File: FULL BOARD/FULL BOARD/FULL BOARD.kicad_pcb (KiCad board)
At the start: 2 copper layers, 200 x 200 mm, 113 parts, among them IC1 TAS5760LDAP, J1 PJ-036AH-SMT-TR, J2 Micro_SD_Card, J3 B2B-PH-K-S, J4 5019514000, J5 61201021621, J6 B2B-PH-K-S, SW1 PTS645SK50SMTR92LFS, U1 LD1117S33TR_SOT223, U2 STM32H743VITx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

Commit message: parts moved
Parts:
- moved J4 68.4 mm to (251.3, 100.4), turned to -90 degrees
- moved J2 52.0 mm to (196.2, 53.8)
- moved C1 45.9 mm to (202.4, 65.4), turned to 0 degrees
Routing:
- net +5V: track 299.4 -> 397.5 mm
- net /SD_DO: track 118.8 -> 64.0 mm
- net /LCD_MOSI: track 50.5 -> 102.3 mm
- net /SD_CLK: track 121.8 -> 70.0 mm
- net /LCD_MISO: track 50.5 -> 101.6 mm
- net Wait: track 53.2 -> 102.6 mm
- net /LCD_CS: track 49.7 -> 97.8 mm
- net /SD_CS: track 125.4 -> 78.3 mm
- net /SD_DI: track 109.3 -> 62.2 mm
- net /LCD_SCK: track 50.9 -> 97.4 mm
- net +3.3V: track 583.7 -> 618.9 mm
- net GND: track 145.4 -> 125.7 mm
- net /NRST: track 126.0 -> 120.4 mm
- net +3.3VA: track 56.4 -> 58.9 mm
- net GNDA: track 38.8 -> 38.1 mm

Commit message: added names
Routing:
- net GND: track 125.7 -> 126.8 mm
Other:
- board text added: "ECE 477 Group 7 Conundrum Crack V 1.0 Colby Acton Joseph Eisenberg Aloysius Rebeiro Andrew Pohl"

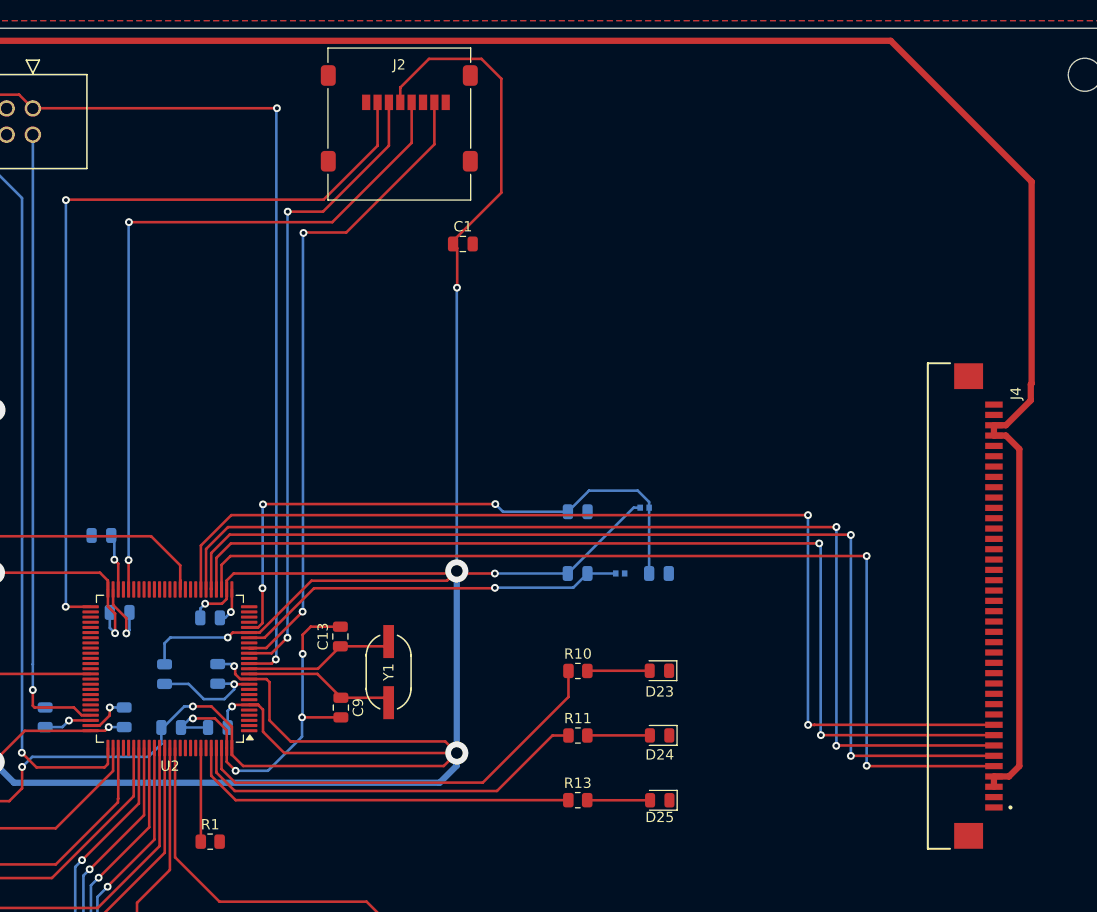
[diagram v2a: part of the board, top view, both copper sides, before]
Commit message: moved sd and lcd
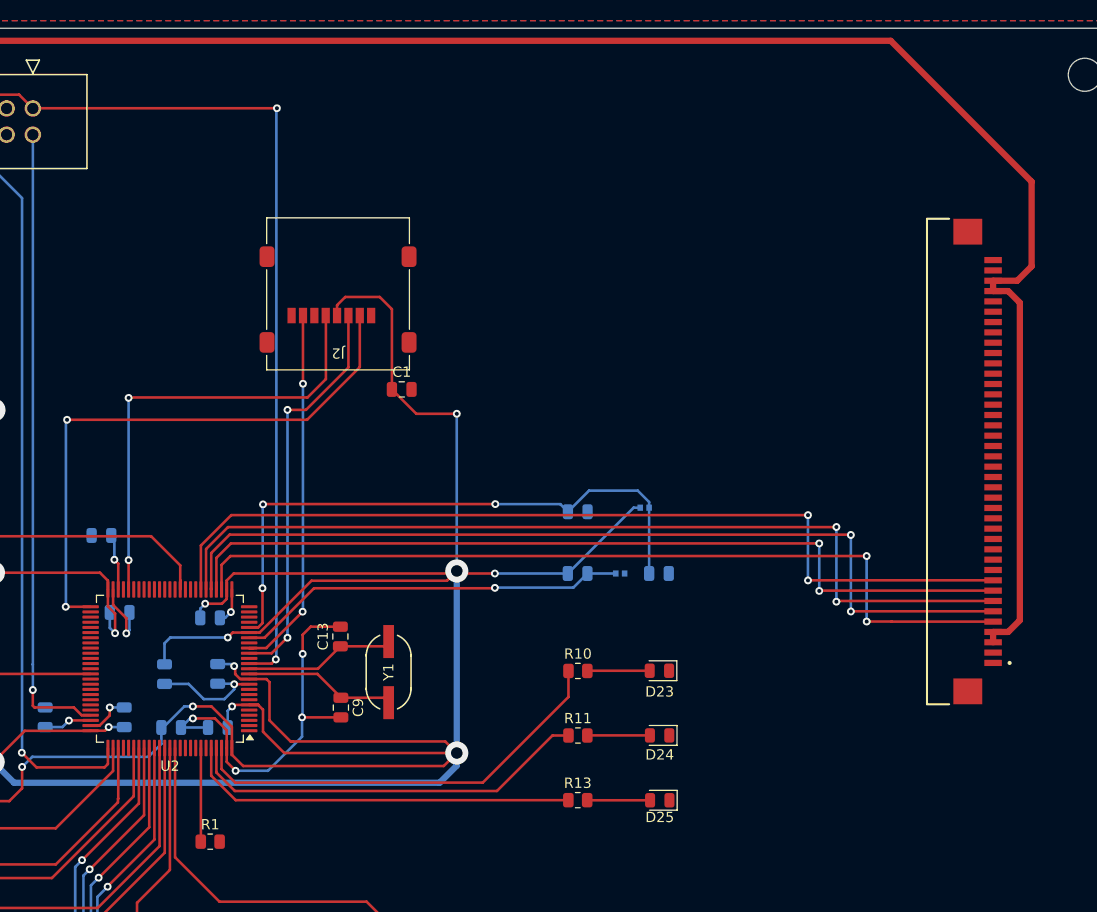
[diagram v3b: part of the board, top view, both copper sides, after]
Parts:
- moved J2 17.5 mm to (190.3, 70.2), turned to 180 degrees
- moved C1 15.3 mm to (196.5, 79.5)
- moved J4 14.0 mm to (251.3, 86.4)
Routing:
- net /SD_DO: track 64.0 -> 35.7 mm
- net /SD_CLK: track 70.0 -> 44.6 mm
- net +3.3V: track 618.9 -> 593.5 mm
- net /SD_DI: track 62.2 -> 39.1 mm
- net /SD_CS: track 78.3 -> 56.0 mm
- net Wait: track 102.6 -> 88.5 mm
- net /LCD_MISO: track 101.6 -> 87.5 mm
- net /LCD_CS: track 97.8 -> 83.8 mm
- net /LCD_MOSI: track 102.3 -> 88.2 mm
- net /LCD_SCK: track 97.4 -> 83.7 mm
- net +5V: track 397.5 -> 384.5 mm

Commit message: moved parts
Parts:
- moved C1 1.16 mm to (196.5, 80.6)
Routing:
- net +3.3V: track 593.5 -> 594.5 mm
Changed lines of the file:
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@@
 	(footprint "Capacitor_SMD:C_0805_2012Metric"
 		(layer "F.Cu")
-		(at 196.47 79.46)
+		(at 196.47 80.62)
 		(descr "Capacitor SMD 0805 (2012 Metric), square (rectangular) end terminal, IPC_7351 nominal, (Body size source: IPC-SM-782 page 76, https://www.pcb-3d.com/wordpress/wp-content/uploads/ipc-sm-782a_amendment_1_and_2.pdf, https://docs.google.com/spreadsheets/d/1BsfQQcO9C6DZCsRaXUlFlo91Tg2WpOkGARC1WS5S8t0/edit?usp=sharing), generated with kicad-footprint-generator")
 		(tags "capacitor")
@@
 	)
 	(segment
-		(start 194.34 70.51)
-		(end 191.006 70.51)
-		(width 0.254)
-		(layer "F.Cu")
-		(net 1)
-	)
-	(segment
 		(start 104.71 131.65)
 		(end 104.7068 131.6532)
@@
 	)
 	(segment
+		(start 190.21 71.306)
+		(end 190.21 72.31)
+		(width 0.254)
+		(layer "F.Cu")
+		(net 1)
+	)
+	(segment
 		(start 89.591 75.1888)
 		(end 89.591 71.7246)
@@
 	)
 	(segment
-		(start 201.8 81.82)
-		(end 197.88 81.82)
+		(start 195.52 80.62)
+		(end 195.52 71.69)
 		(width 0.254)
 		(layer "F.Cu")
@@
 	)
 	(segment
-		(start 195.52 71.69)
-		(end 194.34 70.51)
+		(start 201.5528 97.282)
+		(end 180.200408 97.282)
 		(width 0.254)
 		(layer "F.Cu")
@@
 	)
 	(segment
-		(start 201.5528 97.282)
-		(end 180.200408 97.282)
+		(start 195.52 81.47)
+		(end 195.52 80.62)
 		(width 0.254)
 		(layer "F.Cu")
@@
 	)
 	(segment
-		(start 197.88 81.82)
-		(end 195.52 79.46)
+		(start 194.34 70.51)
+		(end 191.006 70.51)
 		(width 0.254)
 		(layer "F.Cu")
@@
 	)
 	(segment
+		(start 191.006 70.51)
+		(end 190.21 71.306)
+		(width 0.254)
+		(layer "F.Cu")
+		(net 1)
+	)
+	(segment
 		(start 180.831408 107.501)
 		(end 181.702 107.501)
@@
 	)
 	(segment
-		(start 191.006 70.51)
-		(end 190.21 71.306)
-		(width 0.254)
-		(layer "F.Cu")
-		(net 1)
-	)
-	(segment
 		(start 182.572592 110.001)
 		(end 181.702 110.001)
@@
 	)
 	(segment
+		(start 195.52 71.69)
+		(end 194.34 70.51)
+		(width 0.254)
+		(layer "F.Cu")
+		(net 1)
+	)
+	(segment
 		(start 180.027 112.127)
 		(end 180.027 114.176)
@@
 	)
 	(segment
-		(start 195.52 79.46)
-		(end 195.52 71.69)
+		(start 185.1 114.66)
+		(end 183.04 112.6)
 		(width 0.254)
 		(layer "F.Cu")
@@
 	)
 	(segment
-		(start 185.1 114.66)
-		(end 183.04 112.6)
+		(start 181.702 103.001)
+		(end 182.714645 103.001)
 		(width 0.254)
 		(layer "F.Cu")
@@
 	)
 	(segment
-		(start 181.702 103.001)
-		(end 182.714645 103.001)
+		(start 201.8 82.02)
+		(end 196.07 82.02)
 		(width 0.254)
 		(layer "F.Cu")
@@
 	)
 	(segment
-		(start 190.21 71.306)
-		(end 190.21 72.31)
+		(start 196.07 82.02)
+		(end 195.52 81.47)
 		(width 0.254)
 		(layer "F.Cu")
@@
 	)
 	(via
-		(at 201.8 81.82)
+		(at 201.8 82.02)
 		(size 0.762)
 		(drill 0.381)
@@
 	)
 	(segment
-		(start 201.8 97.0348)
-		(end 201.8 81.82)
-		(width 0.254)
-		(layer "B.Cu")
-		(net 1)
-	)
-	(segment
 		(start 201.8 115.88)
 		(end 200.14 117.54)
@@
 		(width 0.254)
 		(layer "B.Cu")
+		(net 1)
+	)
+	(segment
+		(start 201.8 97.0348)
+		(end 201.8 82.02)
+		(width 0.254)
+		(layer "B.Cu")

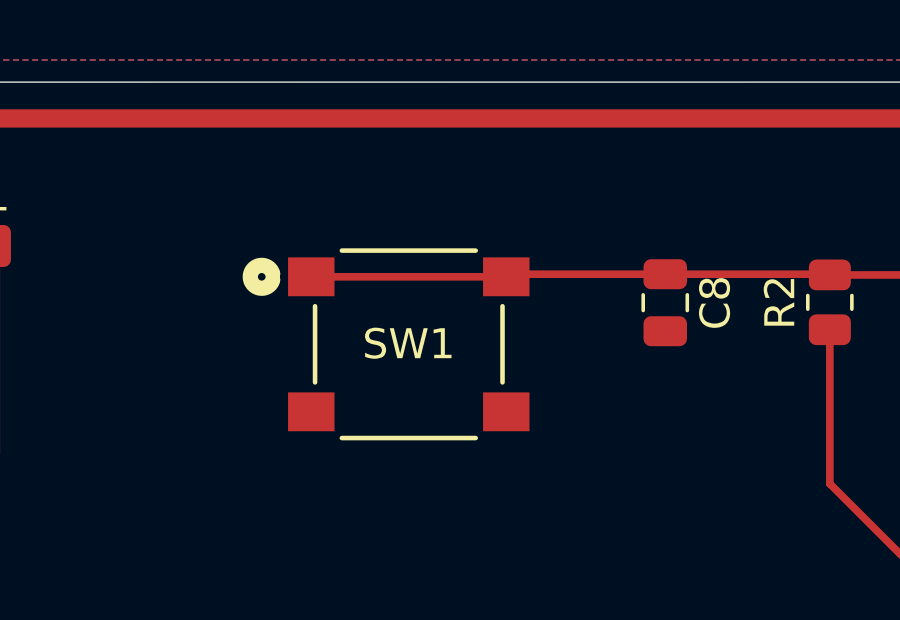
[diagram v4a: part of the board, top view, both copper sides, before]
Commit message: changed reset footprint
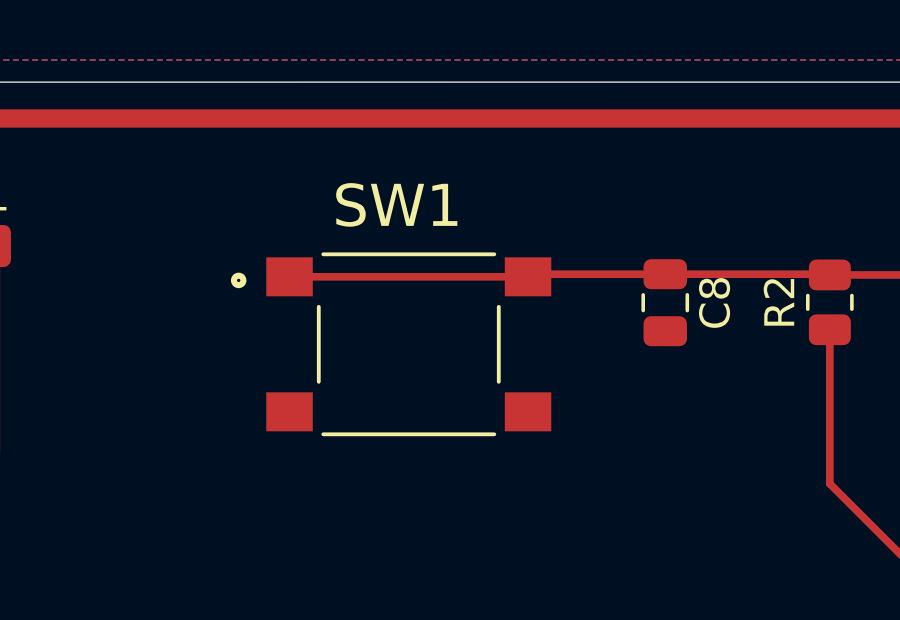
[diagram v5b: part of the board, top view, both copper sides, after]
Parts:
- SW1: footprint push button custom:SW4_PTS645SK50SMTR92LFS_CNK -> Reset Switch:SW_PTS645SK50SMTR92LFS
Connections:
- IC1 pad V: GND -> (no net)
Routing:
- net /NRST: track 120.4 -> 121.1 mm
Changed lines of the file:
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@@
 			(layers "*.Cu" "*.Mask")
 			(remove_unused_layers no)
-			(net 2 "GND")
 		)
 		(model "Z:/Downloads/school/477/KiCAD/PCB-Conundrum-Crack/Footprints/ul_TAS5760LDAP/KiCADv6/TAS5760LDAP.step"
@@
 		)
 	)
-	(footprint "push button custom:SW4_PTS645SK50SMTR92LFS_CNK"
+	(footprint "Reset Switch:SW_PTS645SK50SMTR92LFS"
 		(layer "F.Cu")
 		(at 123.9884 53.2386)
-		(tags "PTS645SK50SMTR92LFS ")
 		(property "Reference" "SW1"
-			(at 0 0 0)
-			(unlocked yes)
+			(at -0.375575 -4.596095 0)
 			(layer "F.SilkS")
 			(effects
 				(font
-					(size 1 1)
+					(size 1.402165 1.402165)
 					(thickness 0.15)
 				)
@@
 		)
 		(property "Value" "PTS645SK50SMTR92LFS"
-			(at 0.1016 5.5914 0)
-			(unlocked yes)
+			(at 15.23461 4.368615 0)
 			(layer "F.Fab")
 			(effects
 				(font
-					(size 1 1)
+					(size 1.402449 1.402449)
 					(thickness 0.15)
 				)
 			)
 		)
-		(property "Footprint" "push button custom:SW4_PTS645SK50SMTR92LFS_CNK"
+		(property "Footprint" "Reset Switch:SW_PTS645SK50SMTR92LFS"
 			(at 0 0 0)
 			(layer "F.Fab")
@@
 		(sheetfile "FULL BOARD.kicad_sch")
 		(attr smd)
-		(fp_circle
-			(center -4.9022 -2.250001)
-			(end -4.5212 -2.250001)
-			(stroke
-				(width 0.508)
-				(type solid)
-			)
-			(fill none)
-			(layer "B.SilkS")
-		)
 		(fp_line
-			(start -3.1242 -1.269561)
-			(end -3.1242 1.269561)
+			(start -3 -1.25)
+			(end -3 1.25)
 			(stroke
-				(width 0.1524)
+				(width 0.127)
 				(type solid)
 			)
@@
 		)
 		(fp_line
-			(start -2.231551 3.1242)
-			(end 2.231551 3.1242)
+			(start -2.85 -3)
+			(end 2.85 -3)
 			(stroke
-				(width 0.1524)
+				(width 0.127)
 				(type solid)
 			)
@@
 		)
 		(fp_line
-			(start 2.231551 -3.1242)
-			(end -2.231551 -3.1242)
+			(start -2.85 3)
+			(end 2.85 3)
 			(stroke
-				(width 0.1524)
+				(width 0.127)
 				(type solid)
 			)
@@
 		)
 		(fp_line
-			(start 3.1242 1.269561)
-			(end 3.1242 -1.269561)
+			(start 3 -1.25)
+			(end 3 1.25)
 			(stroke
-				(width 0.1524)
+				(width 0.127)
 				(type solid)
 			)
 			(layer "F.SilkS")
 		)
-		(fp_arc
-			(start -4.535241 -2.14752)
-			(mid -5.2832 -2.250001)
-			(end -4.535241 -2.352481)
+		(fp_circle
+			(center -5.67 -2.13)
+			(end -5.511888 -2.13)
 			(stroke
-				(width 0.508)
+				(width 0.2)
 				(type solid)
 			)
+			(fill none)
 			(layer "F.SilkS")
 		)
 		(fp_line
-			(start -4.278699 -3.2512)
-			(end -4.278699 3.2512)
+			(start -5 -3.25)
+			(end 5 -3.25)
 			(stroke
-				(width 0.1524)
+				(width 0.05)
 				(type solid)
 			)
@@
 		)
 		(fp_line
-			(start -4.278699 3.2512)
-			(end 4.278699 3.2512)
+			(start -5 3.25)
+			(end -5 -3.25)
 			(stroke
-				(width 0.1524)
+				(width 0.05)
 				(type solid)
 			)
@@
 		)
 		(fp_line
-			(start 4.278699 -3.2512)
-			(end -4.278699 -3.2512)
+			(start 5 -3.25)
+			(end 5 3.25)
 			(stroke
-				(width 0.1524)
+				(width 0.05)
 				(type solid)
 			)
@@
 		)
 		(fp_line
-			(start 4.278699 3.2512)
-			(end 4.278699 -3.2512)
+			(start 5 3.25)
+			(end -5 3.25)
 			(stroke
-				(width 0.1524)
+				(width 0.05)
 				(type solid)
 			)
@@
 		)
 		(fp_line
-			(start -2.9972 -2.9972)
-			(end -2.9972 2.9972)
+			(start -3 -3)
+			(end 3 -3)
 			(stroke
-				(width 0.0254)
+				(width 0.127)
 				(type solid)
 			)
@@
 		)
 		(fp_line
-			(start -2.9972 2.9972)
-			(end 2.9972 2.9972)
+			(start -3 3)
+			(end -3 -3)
 			(stroke
-				(width 0.0254)
+				(width 0.127)
 				(type solid)
 			)
@@
 		)
 		(fp_line
-			(start 2.9972 -2.9972)
-			(end -2.9972 -2.9972)
+			(start 3 -3)
+			(end 3 3)
 			(stroke
-				(width 0.0254)
+				(width 0.127)
 				(type solid)
 			)
@@
 		)
 		(fp_line
-			(start 2.9972 2.9972)
-			(end 2.9972 -2.9972)
+			(start 3 3)
+			(end -3 3)
 			(stroke
-				(width 0.0254)
+				(width 0.127)
 				(type solid)
 			)
@@
 		)
 		(fp_circle
-			(center -3.250001 -4.155001)
-			(end -2.869001 -4.155001)
+			(center -2.368 -2.257)
+			(end -2.209888 -2.257)
 			(stroke
-				(width 0.508)
+				(width 0.2)
 				(type solid)
 			)
@@
 			(layer "F.Fab")
 		)
-		(fp_text user "${REFERENCE}"
-			(at 0 0 0)
-			(unlocked yes)
-			(layer "F.Fab")
-			(effects
-				(font
-					(size 1 1)
-					(thickness 0.15)
-				)
-			)
-		)
 		(pad "1" smd rect
-			(at -3.250001 -2.250001)
-			(size 1.5494 1.2954)
+			(at -3.975 -2.25)
+			(size 1.55 1.3)
 			(layers "F.Cu" "F.Paste" "F.Mask")
 			(net 6 "/NRST")
 			(pinfunction "1")
 			(pintype "unspecified")
+			(solder_mask_margin 0.102)
 		)
 		(pad "2" smd rect
-			(at 3.250001 -2.250001)
-			(size 1.5494 1.2954)
+			(at 3.975 -2.25)
+			(size 1.55 1.3)
 			(layers "F.Cu" "F.Paste" "F.Mask")
 			(net 6 "/NRST")
 			(pinfunction "2")
 			(pintype "unspecified")
+			(solder_mask_margin 0.102)
 		)
 		(pad "3" smd rect
-			(at -3.250001 2.250001)
-			(size 1.5494 1.2954)
+			(at -3.975 2.25)
+			(size 1.55 1.3)
 			(layers "F.Cu" "F.Paste" "F.Mask")
 			(net 2 "GND")
 			(pinfunction "3")
 			(pintype "unspecified")
+			(solder_mask_margin 0.102)
 		)
 		(pad "4" smd rect
-			(at 3.250001 2.250001)
-			(size 1.5494 1.2954)
+			(at 3.975 2.25)
+			(size 1.55 1.3)
 			(layers "F.Cu" "F.Paste" "F.Mask")
 			(net 2 "GND")
 			(pinfunction "4")
 			(pintype "unspecified")
+			(solder_mask_margin 0.102)
 		)
 	)
@@
 		(tags "capacitor")
 		(property "Reference" "C1"
-			(at 0 -1.68 360)
+			(at 0 -1.68 0)
 			(layer "F.SilkS")
 			(effects
@@
 		)
 		(property "Value" "100uF"
-			(at 0 1.68 360)
+			(at 0 1.68 0)
 			(layer "F.Fab")
 			(hide yes)
@@
 		)
 		(fp_text user "${REFERENCE}"
-			(at 0 0 360)
+			(at 0 0 0)
 			(layer "F.Fab")
 			(effects
@@
 	)
 	(segment
+		(start 132.5372 50.9016)
+		(end 128.0504 50.9016)
+		(width 0.254)
+		(layer "F.Cu")
+		(net 6)
+	)
+	(segment
 		(start 183.879 106.001)
 		(end 181.702 106.001)
@@
 	)
 	(segment
-		(start 160.78 52.24)
-		(end 160.76 52.26)
+		(start 127.9634 50.9886)
+		(end 120.0134 50.9886)
 		(width 0.254)
 		(layer "F.Cu")
@@
 	)
 	(segment
-		(start 137.9982 50.9016)
-		(end 138.0236 50.927)
+		(start 160.78 52.24)
+		(end 160.76 52.26)
 		(width 0.254)
 		(layer "F.Cu")
@@
 	)
 	(segment
-		(start 132.5372 50.9016)
-		(end 127.3254 50.9016)
+		(start 137.9982 50.9016)
+		(end 138.0236 50.927)
 		(width 0.254)
 		(layer "F.Cu")
@@
 	)
 	(segment
-		(start 127.3254 50.9016)
-		(end 127.238401 50.988599)
+		(start 128.0504 50.9016)
+		(end 127.9634 50.9886)
 		(width 0.254)
 		(layer "F.Cu")
@@
 		(width 0.254)
 		(layer "F.Cu")
-		(net 6)
-	)
-	(segment
-		(start 127.238401 50.988599)
-		(end 120.738399 50.988599)
-		(width 0.254)
-		(layer "F.Cu")

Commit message: change SD
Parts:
- added J7: MEM2080-00-128-00-A, Second SD card:MEM20800012800A, F.Cu at (7.88, 8.34)
- J2: value Micro_SD_Card -> MEM2080-00-128-00-A; footprint Connector_Card:microSD_HC_Molex_47219-2001 -> Second SD card:MEM20800012800A
- moved J2 3.87 mm to (191.1, 66.4)

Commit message: Added Gerber
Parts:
- removed J7: MEM2080-00-128-00-A, Second SD card:MEM20800012800A
- moved C1 6.18 mm to (202.7, 80.4)
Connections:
- IC1 pad V: (no net) -> GND
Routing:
- net +3.3V: track 594.3 -> 593.7 mm
